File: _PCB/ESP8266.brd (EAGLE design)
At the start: 69.5 x 47 mm, 46 parts, among them IC1 FT232RL, IC2 LD117AS33TR, Q1 12M, T1 S8050, T2 S8050, X1 MINI-USB-32005-201

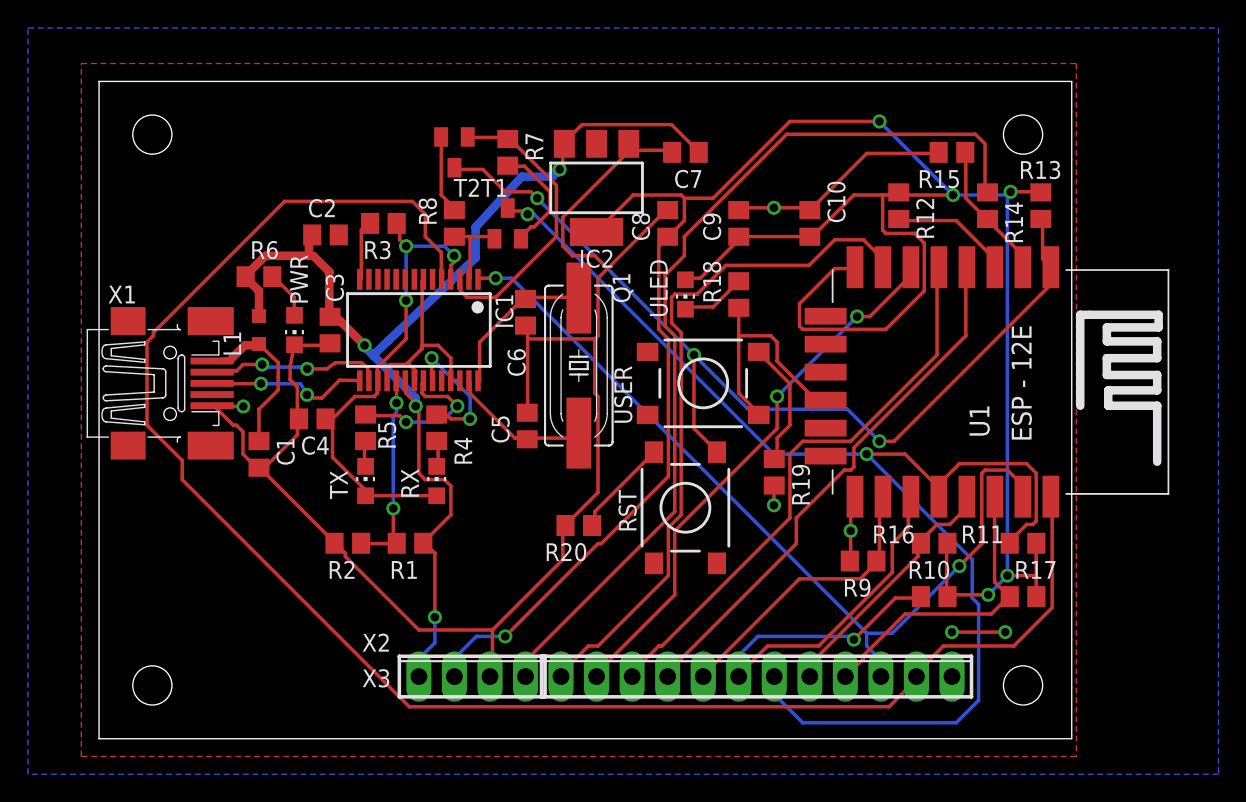
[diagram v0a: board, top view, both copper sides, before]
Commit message: fix transistor pin E/B swap process
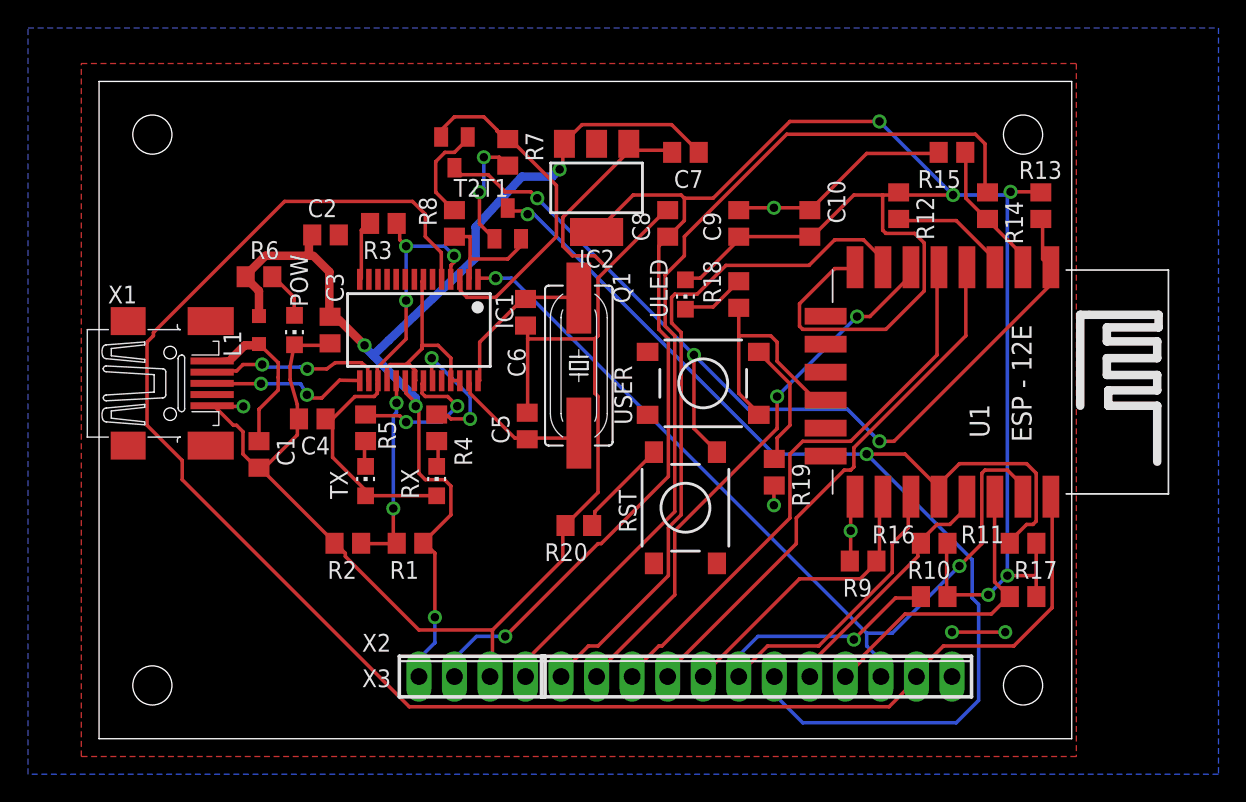
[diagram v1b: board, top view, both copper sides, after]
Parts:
- POW: value PWR -> (none)
- RST: value RST -> (none)
- RX: value RX -> (none)
- T1, T2: device transistor:SOT23-EBC -> transistor:SOT23-BEC
- TX: value TX -> (none)
- USER: value USER -> (none)
- renumbered PWR to POW
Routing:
- net N$17: track 21.2 -> 24.9 mm
- net N$18: track 6.02 -> 8.73 mm
- net N$16: track 5.61 -> 7.33 mm
- net N$15: track 8.14 -> 8.43 mm, vias 0 -> 2
